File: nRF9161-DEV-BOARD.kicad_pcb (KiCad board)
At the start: 4 copper layers, 120 x 80 mm, 103 parts, among them J1 VIN_3V0-5V5, J10 SPI0, J11 I2C0, J12 GPIO_P0.00-15, J13 GPIO_P0.16-31, J14 RFFE_MAGPIO, J15 COEX, J16 I2S, J17 PDM, J18 ADC_AIN0-7, J2 U.FL_LTE_NR+, J3 SWF_LTE, J5 U.FL_GNSS, J6 SWF_GNSS, J7 nanoSIM_4FF, J8 SWD_10pin, J9 UART0, SW1 DISABLE, SW2 RESET, SW3 USER, U1 NRF9161-LACA-R7, U2 TLV73330PDBV, U3 TPS22919DCKR, U4 TPD3F303DPV

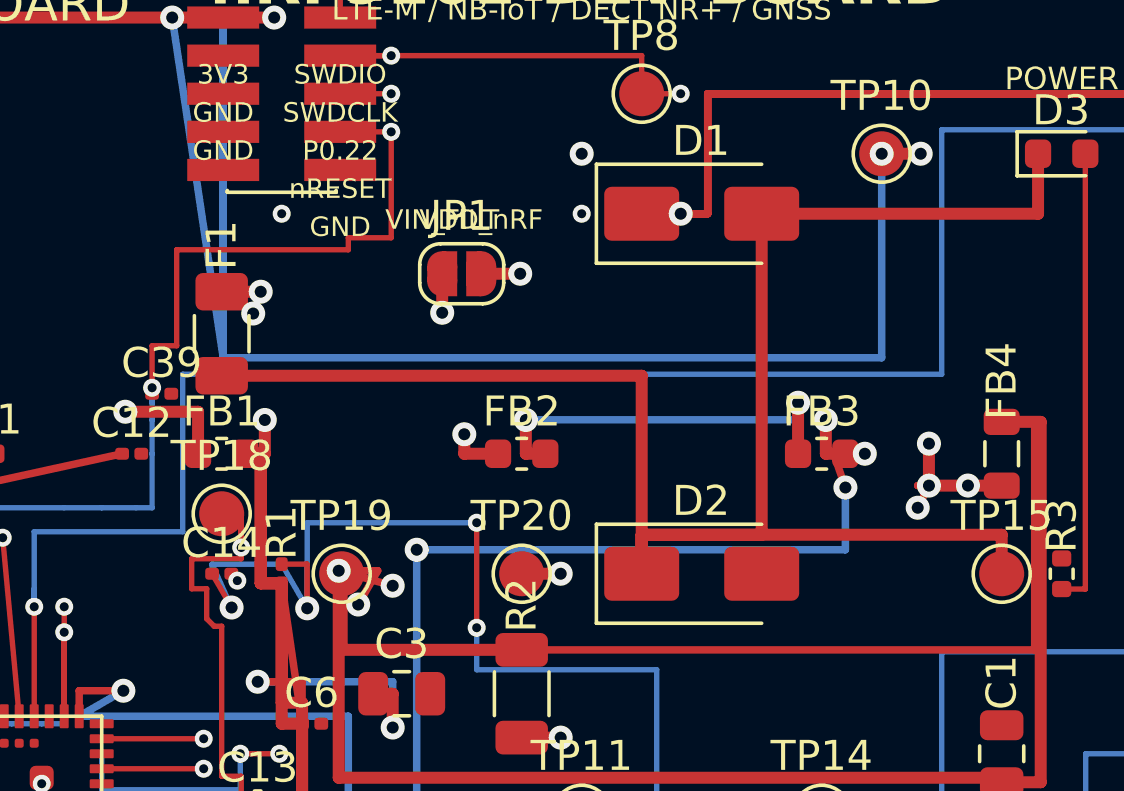
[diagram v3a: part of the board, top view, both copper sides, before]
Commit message: PCB pass30f: close VIN_FILT via ENABLE co-route; unconnected still 78 (GND zone artifact)
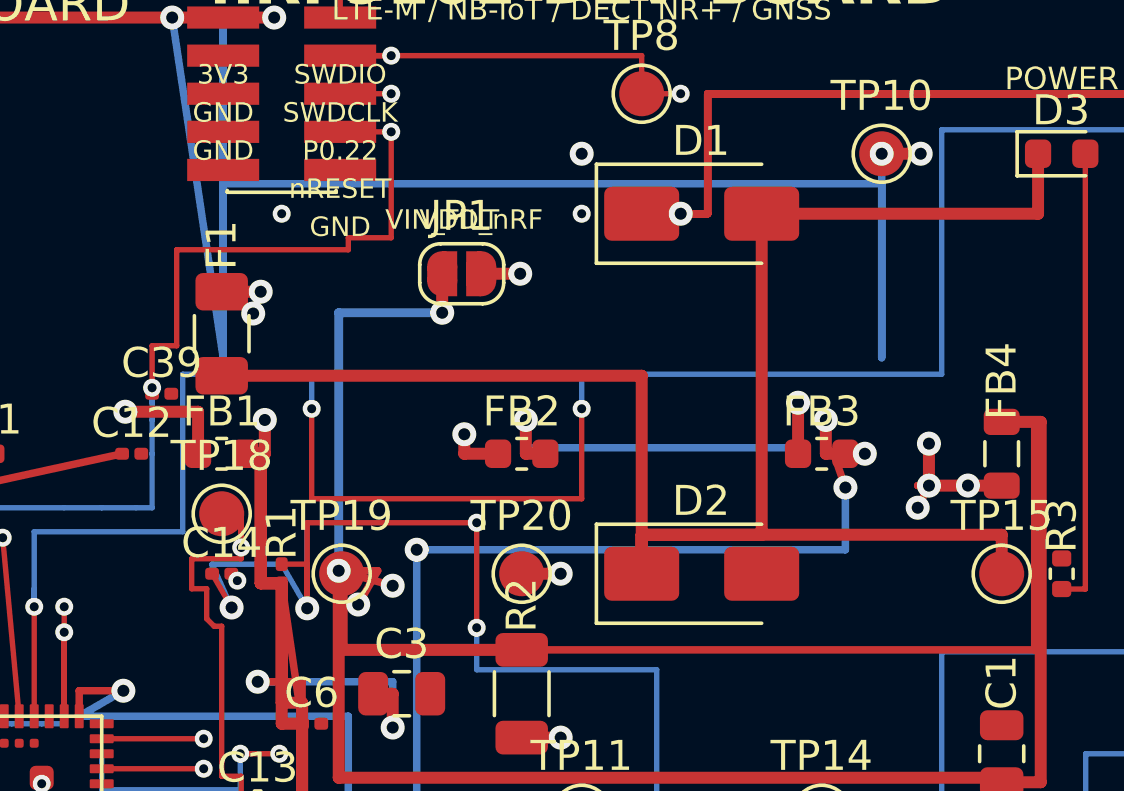
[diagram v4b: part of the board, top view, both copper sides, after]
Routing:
- net VIN_FILT: track 87.7 -> 99.7 mm
- net VDD_GPIO: track 384.0 -> 395.6 mm
- net P0.15: track 316.2 -> 324.5 mm, vias 1 -> 3
- net ENABLE: track 130.0 -> 132.9 mm
- net VDD2_MID: track 13.1 -> 15.0 mm
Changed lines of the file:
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@@
 	)
 	(segment
+		(start 50.85 20.3)
+		(end 56.5 20.3)
+		(width 0.18)
+		(layer "F.Cu")
+		(net 1)
+	)
+	(segment
 		(start 42.75 37.25)
 		(end 42.75 41.1)
@@
 	)
 	(segment
+		(start 50.85 23.15)
+		(end 50.85 20.3)
+		(width 0.18)
+		(layer "F.Cu")
+		(net 1)
+	)
+	(segment
 		(start 56.5 20.3)
 		(end 56.5 23.8)
@@
 	)
 	(segment
-		(start 50.85 20.3)
-		(end 56.5 20.3)
-		(width 0.18)
-		(layer "B.Cu")
-		(net 1)
-	)
-	(segment
 		(start 76.8 36)
 		(end 76.8 28)
@@
 	)
 	(segment
+		(start 48.05 9)
+		(end 48.05 14.8)
+		(width 0.25)
+		(layer "B.Cu")
+		(net 22)
+	)
+	(segment
 		(start 46.64 76)
 		(end 49.18 76)
@@
 	)
 	(segment
+		(start 70 9)
+		(end 48.05 9)
+		(width 0.25)
+		(layer "B.Cu")
+		(net 22)
+	)
+	(segment
 		(start 28.5 40)
 		(end 28.5 19.13)
@@
 	)
 	(segment
-		(start 110.6 38.8)
-		(end 116 38.8)
-		(width 0.4)
+		(start 70 14.8)
+		(end 70 9)
+		(width 0.25)
 		(layer "B.Cu")
 		(net 22)
 	)
 	(segment
-		(start 70 14.8)
-		(end 48.05 14.8)
-		(width 0.25)
+		(start 110.6 38.8)
+		(end 116 38.8)
+		(width 0.4)
 		(layer "B.Cu")
 		(net 22)
@@
 	(segment
 		(start 58.14 16.87)
+		(end 58.14 17.8)
+		(width 0.25)
+		(layer "B.Cu")
+		(net 29)
+	)
+	(segment
+		(start 58.14 17.8)
+		(end 67.21 17.8)
+		(width 0.25)
+		(layer "B.Cu")
+		(net 29)
+	)
+	(segment
+		(start 67.21 17.8)
 		(end 67.21 16.87)
 		(width 0.25)
@@
 	)
 	(segment
+		(start 55.35 13.3)
+		(end 51.9 13.3)
+		(width 0.3)
+		(layer "B.Cu")
+		(net 41)
+	)
+	(segment
+		(start 51.9 13.3)
+		(end 51.9 21.9)
+		(width 0.3)
+		(layer "B.Cu")
+		(net 41)
+	)
+	(segment
 		(start 41.75 26.75)
 		(end 41.75 23.1)
@@
 		(net 42)
 	)
+	(segment
+		(start 51 19.5)
+		(end 60 19.5)
+		(width 0.18)
+		(layer "F.Cu")
+		(net 42)
+	)
+	(segment
+		(start 51 16.5)
+		(end 51 19.5)
+		(width 0.18)
+		(layer "F.Cu")
+		(net 42)
+	)
+	(segment
+		(start 60 19.5)
+		(end 60 16.5)
+		(width 0.18)
+		(layer "F.Cu")
+		(net 42)
+	)
 	(via
 		(at 41.75 23.1)
@@
 		(net 42)
 	)
+	(via
+		(at 60 16.5)
+		(size 0.6)
+		(drill 0.3)
+		(layers "F.Cu" "B.Cu")
+		(net 42)
+	)
+	(via
+		(at 51 16.5)
+		(size 0.6)
+		(drill 0.3)
+		(layers "F.Cu" "B.Cu")
+		(net 42)
+	)
+	(segment
+		(start 60 15.35)
+		(end 72 15.35)
+		(width 0.18)
+		(layer "B.Cu")
+		(net 42)
+	)
 	(segment
 		(start 43.08 77.4)
@@
 	)
 	(segment
+		(start 60 16.5)
+		(end 60 15.35)
+		(width 0.18)
+		(layer "B.Cu")
+		(net 42)
+	)
+	(segment
 		(start 44.1 76)
 		(end 44.1 78.15)
@@
 	)
 	(segment
+		(start 46.7 15.35)
+		(end 51 15.35)
+		(width 0.18)
+		(layer "B.Cu")
+		(net 42)
+	)
+	(segment
 		(start 43.08 78.15)
 		(end 43.08 62)
@@
 	)
 	(segment
-		(start 46.7 15.35)
-		(end 72 15.35)
-		(width 0.18)
-		(layer "B.Cu")
-		(net 42)
-	)
-	(segment
 		(start 44.1 78.15)
 		(end 43.08 78.15)
@@
 		(width 0.18)
 		(layer "B.Cu")
+		(net 42)
+	)
+	(segment
+		(start 51 15.35)
+		(end 51 16.5)
+		(width 0.18)
+		(layer "B.Cu")

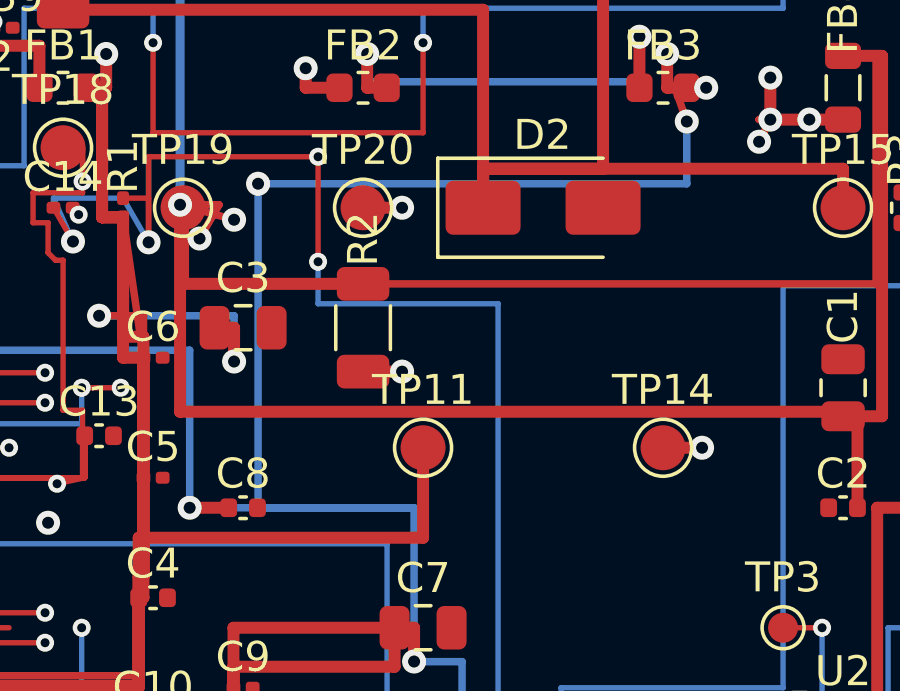
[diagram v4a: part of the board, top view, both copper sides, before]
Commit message: PCB pass30h: VDD2 corridor bridge + VDD_nRF via north; P0.08 restore deferred; unconnected still 78
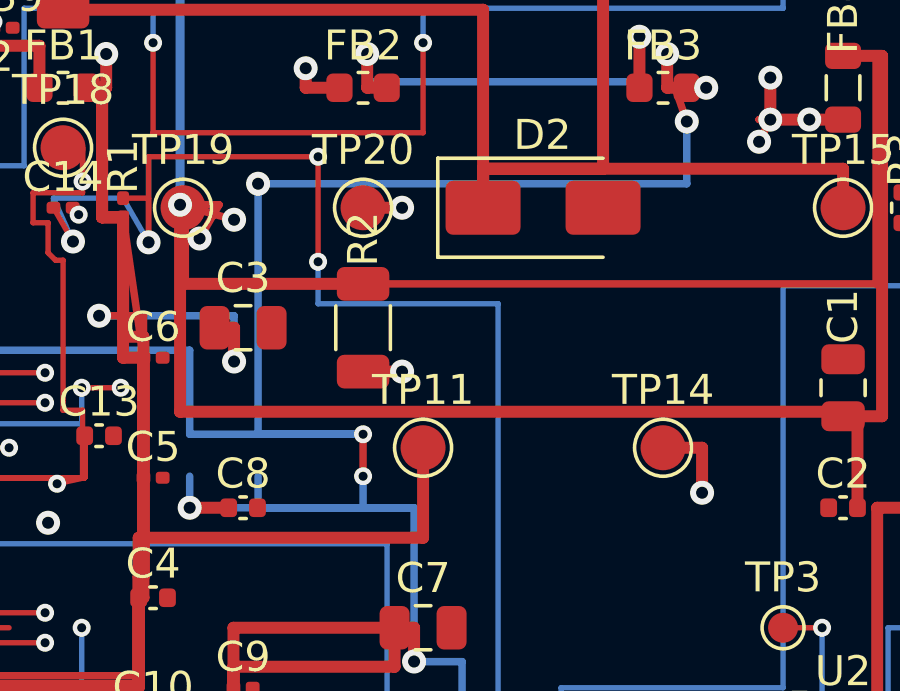
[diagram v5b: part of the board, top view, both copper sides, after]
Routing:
- net VDD2: track 129.7 -> 138.6 mm, vias 9 -> 11
- net VDD_nRF: track 12.1 -> 13.6 mm
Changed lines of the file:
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@@
 	)
 	(segment
-		(start 76.8 36)
-		(end 76.8 28)
-		(width 0.18)
-		(layer "B.Cu")
-		(net 1)
-	)
-	(segment
-		(start 62.5 25.2)
-		(end 62.5 40.95)
+		(start 76.8 28)
+		(end 90.38 28)
 		(width 0.18)
 		(layer "B.Cu")
@@
 	)
 	(segment
-		(start 76.8 28)
-		(end 90.38 28)
+		(start 75.5 36)
+		(end 76.8 36)
 		(width 0.18)
 		(layer "B.Cu")
@@
 	)
 	(segment
-		(start 75.5 36)
-		(end 76.8 36)
+		(start 56.5 23.8)
+		(end 56.5 25.2)
 		(width 0.18)
 		(layer "B.Cu")
@@
 	)
 	(segment
-		(start 56.5 23.8)
-		(end 56.5 25.2)
+		(start 76.8 36)
+		(end 76.8 28)
 		(width 0.18)
 		(layer "B.Cu")
@@
 	)
 	(segment
+		(start 62.5 25.2)
+		(end 62.5 40.95)
+		(width 0.18)
+		(layer "B.Cu")
+		(net 1)
+	)
+	(segment
 		(start 48.33 23.125833)
 		(end 47.68 21.68)
@@
 	)
 	(segment
+		(start 58 29.55)
+		(end 58 30.95)
+		(width 0.25)
+		(layer "F.Cu")
+		(net 39)
+	)
+	(segment
 		(start 53.68 37.3)
 		(end 59.05 37.3)
@@
 	)
 	(via
+		(at 58 30.95)
+		(size 0.6)
+		(drill 0.3)
+		(layers "F.Cu" "B.Cu")
+		(net 39)
+	)
+	(via
 		(at 59.699999 37.125833)
 		(size 0.8)
@@
 	)
 	(via
+		(at 58 29.55)
+		(size 0.6)
+		(drill 0.3)
+		(layers "F.Cu" "B.Cu")
+		(net 39)
+	)
+	(via
 		(at 69.437499 18)
 		(size 0.8)
@@
 	)
 	(segment
+		(start 52.22 30.95)
+		(end 52.22 32)
+		(width 0.25)
+		(layer "B.Cu")
+		(net 39)
+	)
+	(segment
+		(start 58 30.95)
+		(end 58 32)
+		(width 0.25)
+		(layer "B.Cu")
+		(net 39)
+	)
+	(segment
 		(start 52.22 32)
 		(end 59.7 32)
@@
 	)
 	(segment
+		(start 54.5 21.2)
+		(end 54.5 29.55)
+		(width 0.25)
+		(layer "B.Cu")
+		(net 39)
+	)
+	(segment
 		(start 59.7 32)
 		(end 59.7 37.13)
@@
 	)
 	(segment
+		(start 52.22 29.55)
+		(end 58 29.55)
+		(width 0.25)
+		(layer "B.Cu")
+		(net 39)
+	)
+	(segment
+		(start 54.5 30.95)
+		(end 54.5 32)
+		(width 0.25)
+		(layer "B.Cu")
+		(net 39)
+	)
+	(segment
 		(start 68.79 21.2)
 		(end 54.5 21.2)
@@
 	)
 	(segment
+		(start 54.5 29.55)
+		(end 58 29.55)
+		(width 0.25)
+		(layer "B.Cu")
+		(net 39)
+	)
+	(segment
 		(start 61.3 37.13)
 		(end 61.3 42)
@@
 	)
 	(segment
-		(start 54.5 21.2)
-		(end 54.5 32)
+		(start 52.22 26.75)
+		(end 52.22 29.55)
 		(width 0.25)
 		(layer "B.Cu")
@@
 	)
 	(segment
-		(start 52.22 26.75)
-		(end 52.22 32)
-		(width 0.25)
-		(layer "B.Cu")
-		(net 39)
-	)
-	(segment
 		(start 44.722243 25.9)
 		(end 43.25 26.75)
@@
 	)
 	(segment
-		(start 72 38)
-		(end 72 24.6)
-		(width 0.18)
-		(layer "B.Cu")
-		(net 73)
-	)
-	(segment
 		(start 64.599999 43.2)
 		(end 64.599999 38)
@@
 	)
 	(segment
+		(start 72 38)
+		(end 72 24.6)
+		(width 0.18)
+		(layer "B.Cu")
+		(net 73)
+	)
+	(segment
 		(start 37.75 41.1)
 		(end 37.75 33.2)
@@
 	)
 	(segment
+		(start 69.3 30)
+		(end 69.3 31.5)
+		(width 0.4)
+		(layer "F.Cu")
+		(net 75)
+	)
+	(segment
 		(start 58 22)
 		(end 59.3 22)
@@
 	)
 	(via
-		(at 69.3 30)
+		(at 69.3 31.5)
 		(size 0.8)
 		(drill 0.4)

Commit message: PCB pass30i: close P0.08 U1–SW3 island; unconnected 78→77
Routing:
- net P0.08: track 11.3 -> 49.3 mm
- net ENABLE: vias 11 -> 15
- net COEX2: vias 1 -> 3
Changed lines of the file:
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@@
 	)
 	(segment
+		(start 76.8 30.9)
+		(end 79.2 30.9)
+		(width 0.18)
+		(layer "F.Cu")
+		(net 1)
+	)
+	(segment
 		(start 52 44)
 		(end 42.75 44)
@@
 	)
 	(segment
+		(start 62.5 29.6)
+		(end 62.5 30.9)
+		(width 0.18)
+		(layer "F.Cu")
+		(net 1)
+	)
+	(segment
 		(start 56.5 20.3)
 		(end 56.5 23.8)
@@
 	)
 	(via
+		(at 62.5 29.6)
+		(size 0.6)
+		(drill 0.3)
+		(layers "F.Cu" "B.Cu")
+		(net 1)
+	)
+	(via
+		(at 76.8 30.9)
+		(size 0.6)
+		(drill 0.3)
+		(layers "F.Cu" "B.Cu")
+		(net 1)
+	)
+	(via
 		(at 62.5 40.95)
 		(size 0.6)
@@
 	)
 	(via
+		(at 79.2 30.9)
+		(size 0.6)
+		(drill 0.3)
+		(layers "F.Cu" "B.Cu")
+		(net 1)
+	)
+	(via
 		(at 50.85 23.152243)
 		(size 0.8)
@@
 	)
 	(via
+		(at 62.5 30.9)
+		(size 0.6)
+		(drill 0.3)
+		(layers "F.Cu" "B.Cu")
+		(net 1)
+	)
+	(via
 		(at 43.4 45.125833)
 		(size 0.8)
@@
 	)
 	(segment
-		(start 76.8 28)
-		(end 90.38 28)
+		(start 62.5 30.9)
+		(end 62.5 40.95)
+		(width 0.18)
+		(layer "B.Cu")
+		(net 1)
+	)
+	(segment
+		(start 79.2 30.9)
+		(end 79.2 28)
+		(width 0.18)
+		(layer "B.Cu")
+		(net 1)
+	)
+	(segment
+		(start 76.8 36)
+		(end 76.8 30.9)
+		(width 0.18)
+		(layer "B.Cu")
+		(net 1)
+	)
+	(segment
+		(start 62.5 25.2)
+		(end 62.5 29.6)
 		(width 0.18)
 		(layer "B.Cu")
@@
 	)
 	(segment
-		(start 76.8 36)
-		(end 76.8 28)
+		(start 79.2 28)
+		(end 90.38 28)
 		(width 0.18)
 		(layer "B.Cu")
@@
 	)
 	(segment
-		(start 62.5 25.2)
-		(end 62.5 40.95)
-		(width 0.18)
-		(layer "B.Cu")
-		(net 1)
-	)
-	(segment
 		(start 48.33 23.125833)
 		(end 47.68 21.68)
@@
 	)
 	(segment
+		(start 78.5 26)
+		(end 79.67 26)
+		(width 0.18)
+		(layer "B.Cu")
+		(net 61)
+	)
+	(segment
+		(start 46.2 30)
+		(end 46.2 30.25)
+		(width 0.18)
+		(layer "B.Cu")
+		(net 61)
+	)
+	(segment
+		(start 78.5 30.25)
+		(end 78.5 26)
+		(width 0.18)
+		(layer "B.Cu")
+		(net 61)
+	)
+	(segment
+		(start 46.2 30.25)
+		(end 78.5 30.25)
+		(width 0.18)
+		(layer "B.Cu")
+		(net 61)
+	)
+	(segment
 		(start 8 40)
 		(end 8 43.6)
@@
 	)
 	(segment
+		(start 72 30.9)
+		(end 72 29.6)
+		(width 0.18)
+		(layer "F.Cu")
+		(net 73)
+	)
+	(segment
 		(start 37.75 37.25)
 		(end 37.75 41.1)
@@
 	)
 	(via
+		(at 72 30.9)
+		(size 0.6)
+		(drill 0.3)
+		(layers "F.Cu" "B.Cu")
+		(net 73)
+	)
+	(via
 		(at 37.75 41.1)
 		(size 0.6)
@@
 		(net 73)
 	)
+	(via
+		(at 72 29.6)
+		(size 0.6)
+		(drill 0.3)
+		(layers "F.Cu" "B.Cu")
+		(net 73)
+	)
 	(segment
 		(start 72 24.6)
@@
 	)
 	(segment
+		(start 72 38)
+		(end 72 30.9)
+		(width 0.18)
+		(layer "B.Cu")
+		(net 73)
+	)
+	(segment
 		(start 58.8 33.2)
 		(end 58.8 43.2)
@@
 	)
 	(segment
-		(start 72 38)
+		(start 72 29.6)
 		(end 72 24.6)
 		(width 0.18)
